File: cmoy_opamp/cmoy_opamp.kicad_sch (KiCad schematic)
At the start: 51 parts, among them J1 AudioJack3, J2 AudioJack3, SW1 SPST, U1 MC33178, U2 LMH6642, U3 LMH6642, U4 LMH6642

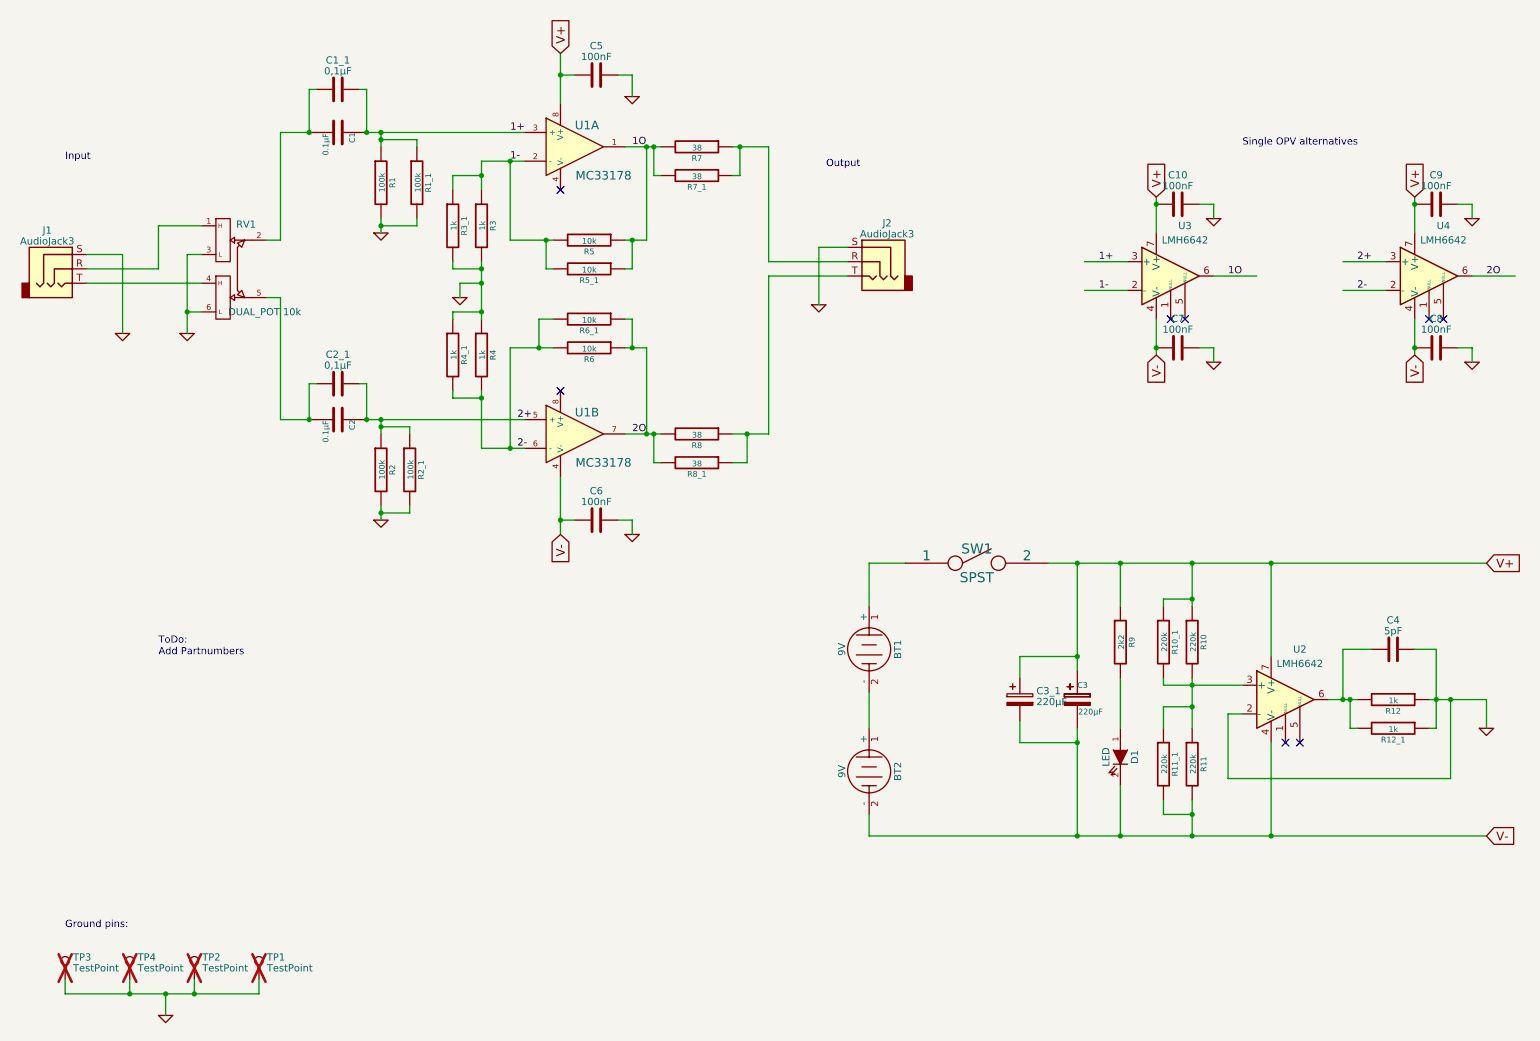
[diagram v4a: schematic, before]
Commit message: replace some rescue lib symbols with built in ones
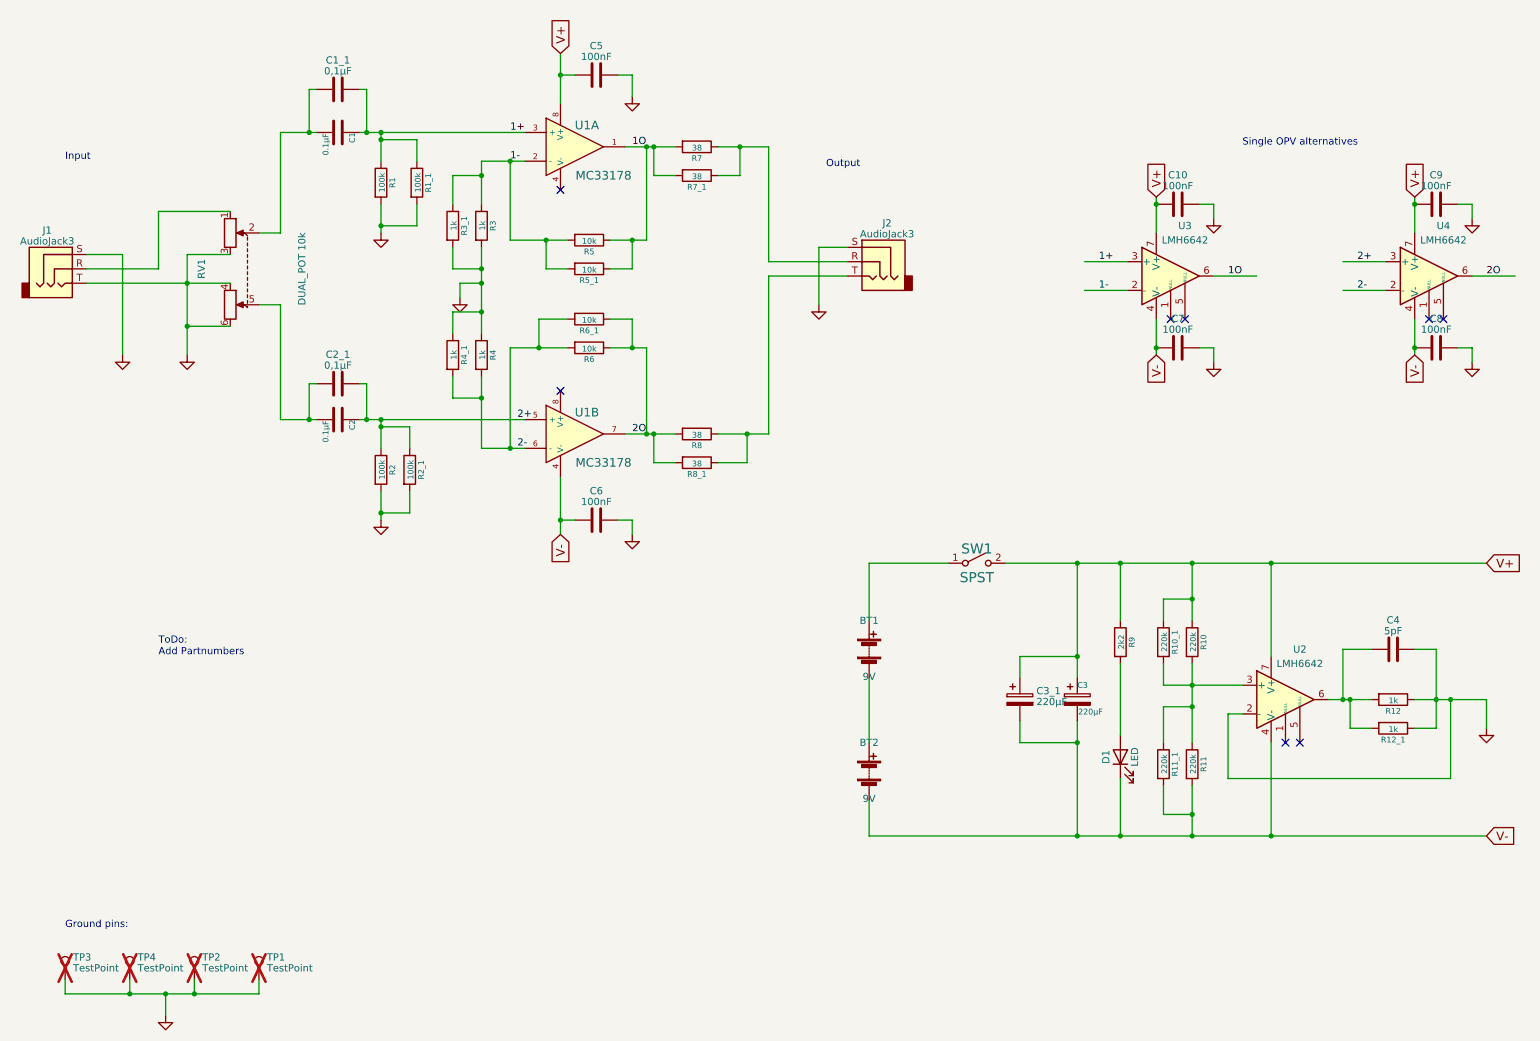
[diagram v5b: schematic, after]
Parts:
- BT1, BT2: symbol d2k2_cmoy-rescue:BATTERY -> Device:Battery
- C1, C2: symbol d2k2_cmoy-rescue:C -> Device:C
- C3: symbol d2k2_cmoy-rescue:CP2 -> Device:C_Polarized
- D1: symbol d2k2_cmoy-rescue:LED -> Device:LED
- R1, R10, R10_1, R11, R11_1, R12, R12_1, R1_1, R2, R2_1, R3, R3_1, R4, R4_1, R5, R5_1, R6, R6_1, R7, R7_1, R8, R8_1, R9: symbol d2k2_cmoy-rescue:R -> Device:R
- RV1: symbol d2k2_cmoy-rescue:DUAL_POT -> Device:R_Potentiometer_Dual
- SW1: symbol d2k2_cmoy-rescue:SPST -> Switch:SW_SPST
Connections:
- net GND: now also J1.T, RV1.4
- net V-: now also D1.1 (K); no longer D1.2 (K)
- net at R9.2: now also D1.2 (A); no longer D1.1 (A)

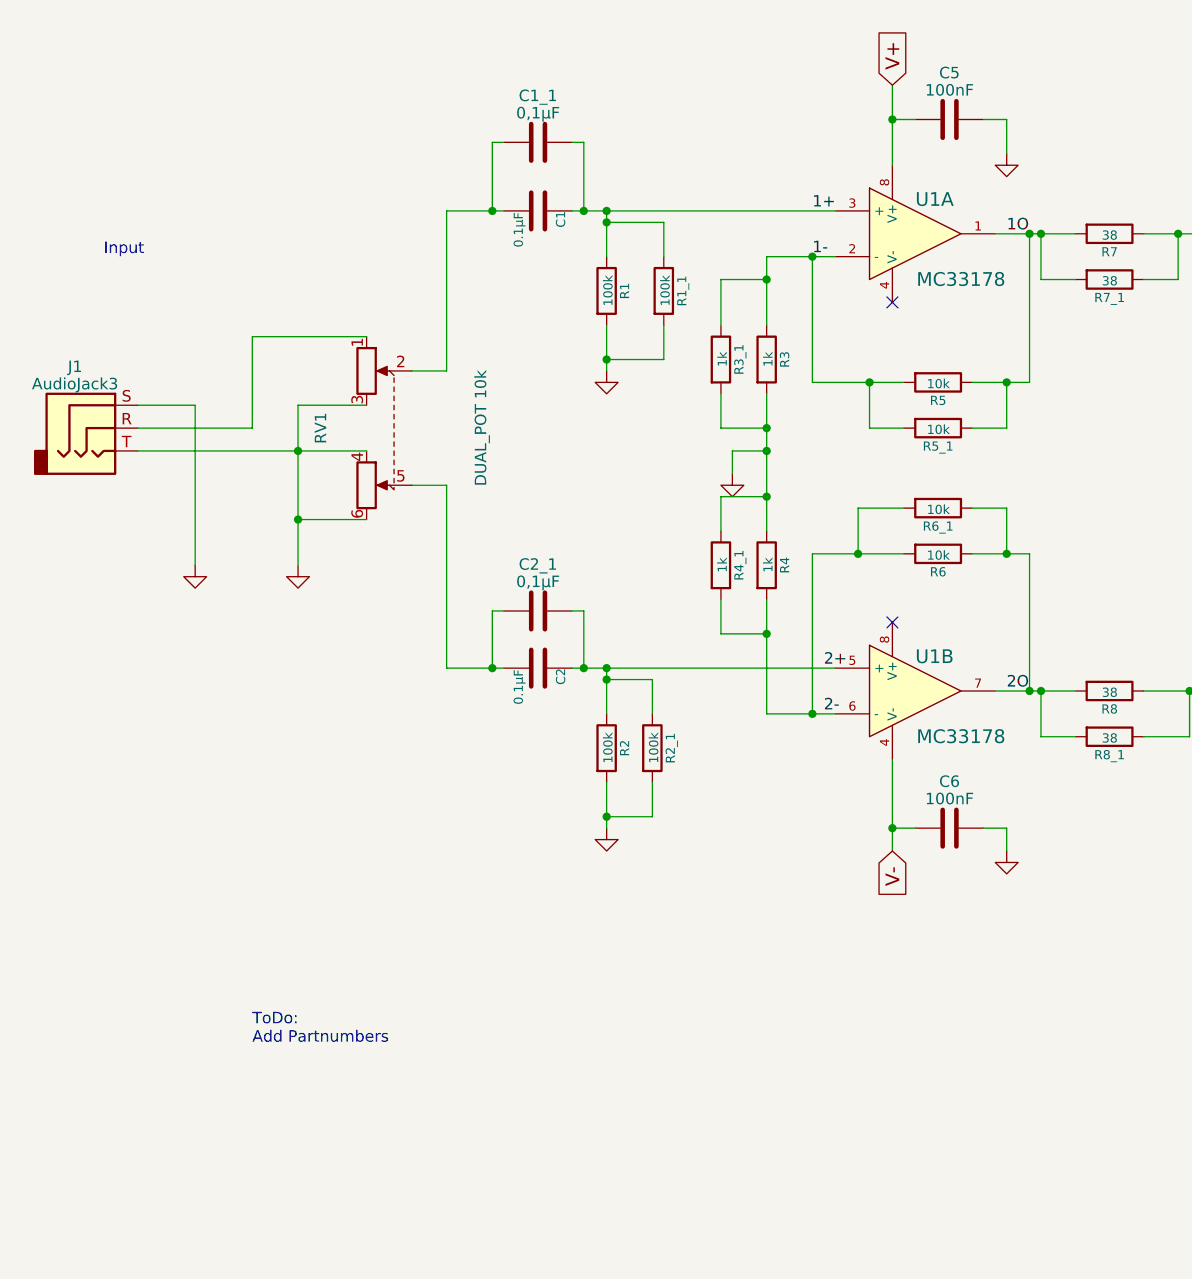
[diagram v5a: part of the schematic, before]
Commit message: fully remove rescue lib reference
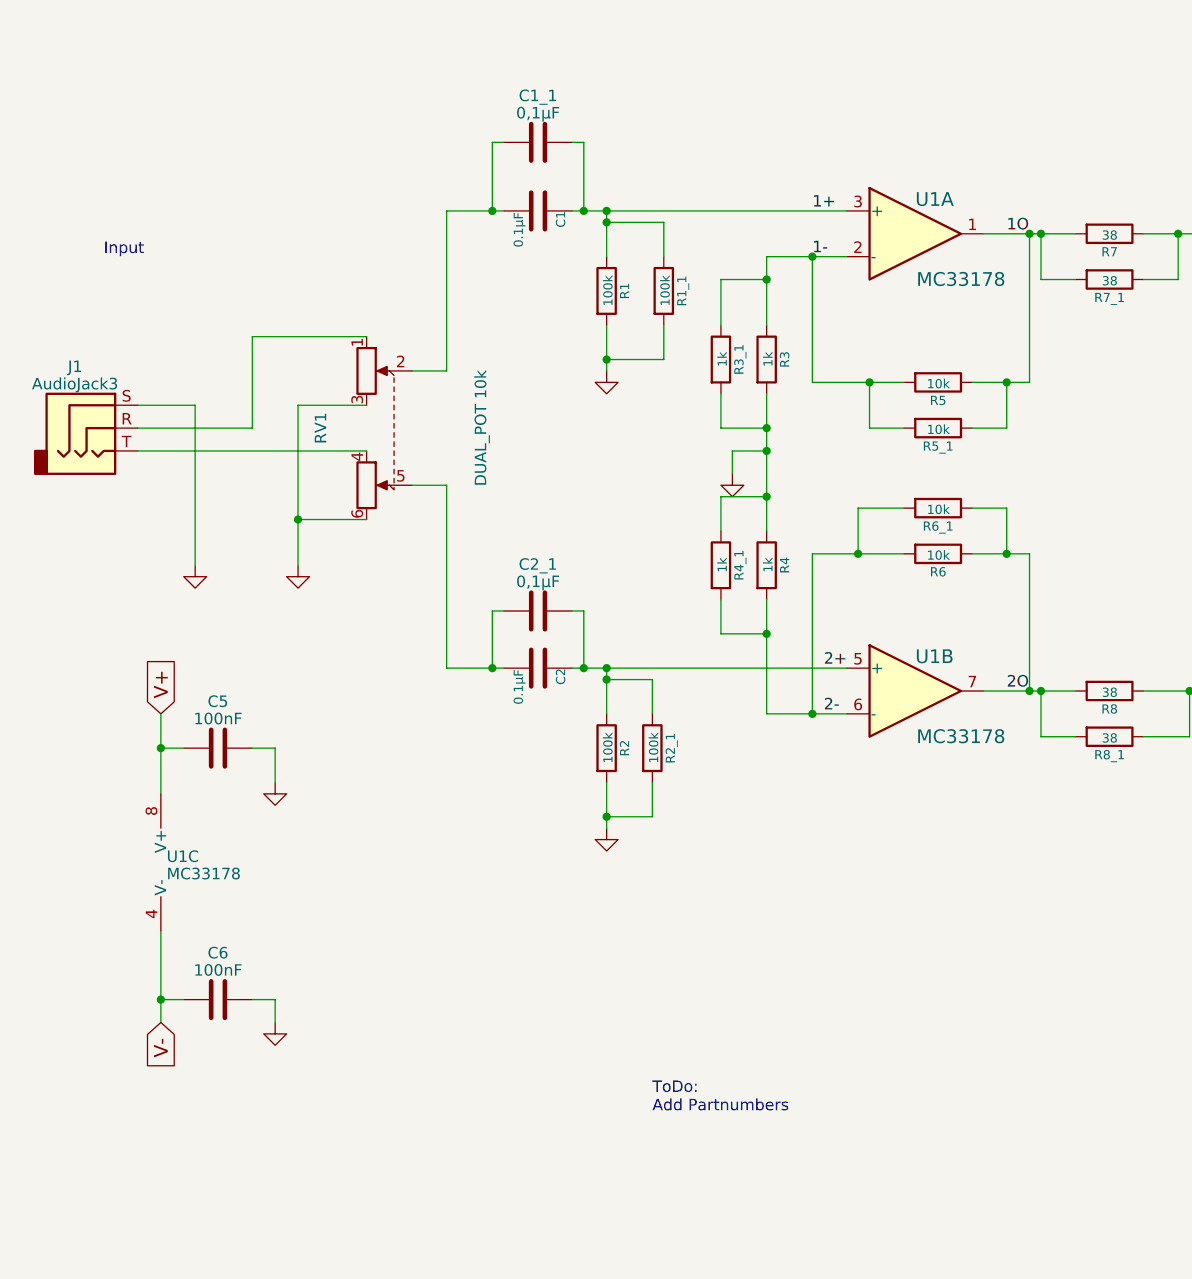
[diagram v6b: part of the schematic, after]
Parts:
- added unit 3 of U1
- U1: symbol d2k2_cmoy-rescue:MC33178 -> Amplifier_Operational:MC33178
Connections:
- net GND: no longer J1.T, RV1.4
- net V+: now also U1.8 (V+); no longer U1.8 (V+)
- net V-: now also U1.4 (V-); no longer U1.4 (V-)
- new net: J1.T, RV1.4
- no-connect marks 8 -> 6
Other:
- moved on the sheet: C5, C6
